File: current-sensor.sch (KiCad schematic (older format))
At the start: 36 parts, among them J1 ‎0197134001‎, J2 ‎0197134001‎, J3 0731000105, J4 Molex_SL_01x02_Male, J5 Molex_SL_01x02_Male, SW1 PN12SHNA03QE, SW2 OS103011MA7QP1, SW3 OS103011MA7QP1, U1 ACS730xLCTR-40AB, U2 AD8616xRM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

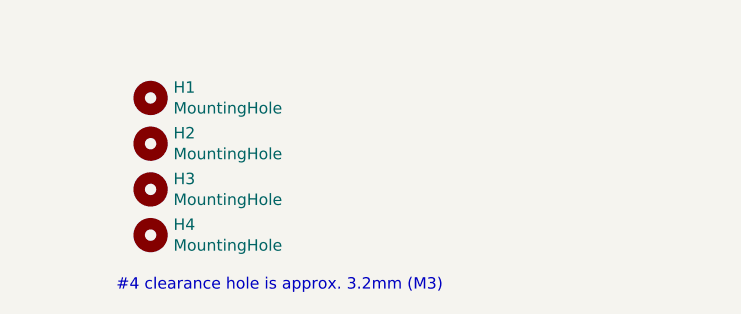
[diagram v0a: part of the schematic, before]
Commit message: remove note about #4 clearance hole size
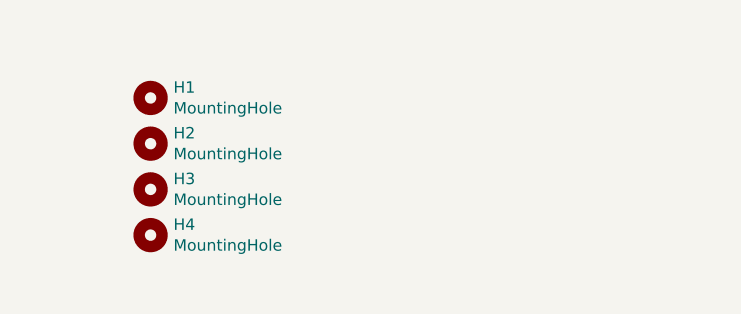
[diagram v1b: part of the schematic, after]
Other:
- note removed: "#4 clearance hole is approx. 3.2mm (M3)"
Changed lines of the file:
@@
 Text Notes 2400 1450 0    50   ~ 10
 to 9V battery
-Text Notes 950  8000 0    50   ~ 0
-#4 clearance hole is approx. 3.2mm (M3)
 $Comp
 L Graphic_gkeeth:Logo_MadeWithKiCad LOGO2
